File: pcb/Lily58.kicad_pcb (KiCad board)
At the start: 2 copper layers, 142.5 x 106.3 mm, 123 parts, among them J1 LED, J2 4PIN, P1 i2c_pin, P2 i2c_pin, P3 ICSP, P4 OLED, SW1 SW_PUSH, SW10 SW_PUSH, SW11 SW_PUSH, SW12 SW_PUSH, SW13 SW_PUSH, SW14 SW_PUSH, SW15 SW_PUSH, SW16 SW_PUSH, SW17 SW_PUSH, SW18 SW_PUSH, SW19 SW_PUSH, SW2 SW_PUSH, SW20 SW_PUSH, SW21 SW_PUSH, SW22 SW_PUSH, SW23 SW_PUSH, SW24 SW_PUSH, SW25 SW_PUSH, SW26 SW_PUSH, SW27 SW_PUSH, SW28 SW_PUSH, SW29 SW_PUSH, SW3 SW_PUSH, SW4 SW_PUSH, SW5 SW_PUSH, SW6 SW_PUSH, SW7 SW_PUSH, SW8 SW_PUSH, SW9 SW_PUSH, U1 ProMicro

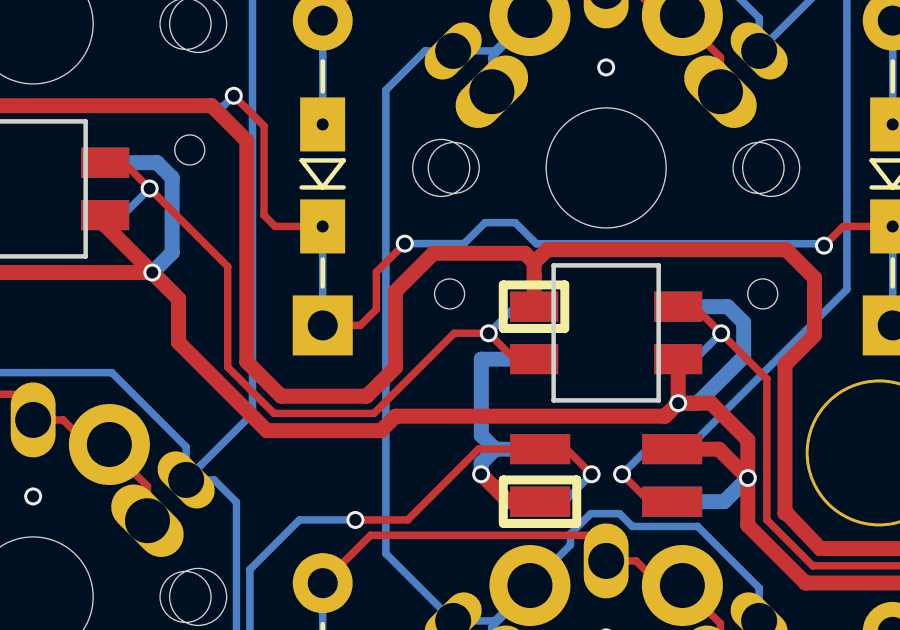
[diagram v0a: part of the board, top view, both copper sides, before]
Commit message: Uodate VCC connection on underglow LED
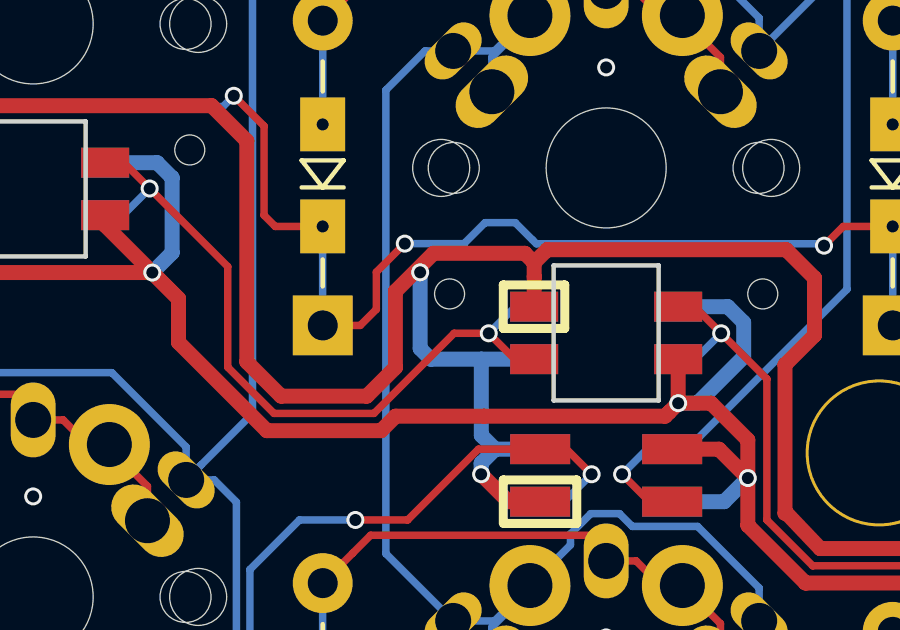
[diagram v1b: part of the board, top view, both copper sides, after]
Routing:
- net VCC: track 1030.4 -> 1035.1 mm, vias 43 -> 44
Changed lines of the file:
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@@
-(kicad_pcb (version 20171130) (host pcbnew "(6.0.0-rc1-dev-1672-g5c3f6f2ab)")
+(kicad_pcb (version 20171130) (host pcbnew "(5.1.4)-1")
   (general
     (thickness 1.6)
     (drawings 251)
-    (tracks 3126)
+    (tracks 3131)
     (zones 0)
     (modules 123)
@@
   (segment (start 193.987476 93.345) (end 190.9445 93.345) (width 0.5) (layer F.Cu) (net 34))
   (segment (start 188.722 98.1075) (end 185.8645 98.1075) (width 0.5) (layer F.Cu) (net 34))
+  (segment (start 192.538998 96.875) (end 190.855 96.875) (width 0.5) (layer B.Cu) (net 34))
+  (segment (start 190.855 96.875) (end 190.5 96.52) (width 0.5) (layer B.Cu) (net 34))
+  (segment (start 190.5 96.52) (end 190.5 93.98) (width 0.5) (layer B.Cu) (net 34))
+  (segment (start 190.5 93.98) (end 190.5 93.98) (width 0.5) (layer B.Cu) (net 34))
+  (via (at 190.5 93.98) (size 0.6) (drill 0.4) (layers F.Cu B.Cu) (net 34))
   (segment (start 84.15 45.6) (end 90.1 45.6) (width 0.5) (layer F.Cu) (net 35))
   (segment (start 93.25763 48.75) (end 93.389884 48.617746) (width 0.5) (layer F.Cu) (net 35))
